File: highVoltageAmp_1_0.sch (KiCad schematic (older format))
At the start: 18 parts, among them U2 OPA211, U3 OPA211

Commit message: Final production board v1.0
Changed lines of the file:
@@
 EESchema Schematic File Version 2
+LIBS:MicroFLiC_DAC_1_0-rescue
 LIBS:power
 LIBS:device
@@
 $EndComp
 Wire Wire Line
-	2800 4000 3050 4000
-Wire Wire Line
-	2800 2800 2800 4150
-Wire Wire Line
-	2800 2800 2900 2800
+	2800 4000 3150 4000
+Wire Wire Line
+	2800 2800 2800 4250
+Wire Wire Line
+	2800 2800 3100 2800
 Connection ~ 2800 4000
 Wire Wire Line
-	3900 2700 4700 2700
-Wire Wire Line
-	4200 2700 4200 4000
-Wire Wire Line
-	4200 4000 3550 4000
-Wire Wire Line
-	2800 4650 2800 4750
+	3700 2700 4700 2700
+Wire Wire Line
+	4200 4000 4200 2700
+Wire Wire Line
+	3450 4000 4200 4000
+Wire Wire Line
+	2800 4550 2800 4750
 $Comp
 L GNDA #PWR031
@@
 U 1 1 55733A0C
 P 3300 4300
+AR Path="/55733A0C" Ref="C14"  Part="1"
+AR Path="/5573337B/55733A0C" Ref="C14"  Part="1"
 F 0 "C14" H 3350 4400 50  0000 L CNN
 F 1 "(10p)" H 3350 4200 50  0000 L CNN
@@
 $EndComp
 Wire Wire Line
-	3500 4300 3650 4300
+	3450 4300 3650 4300
 Wire Wire Line
 	3650 4300 3650 4000
 Connection ~ 3650 4000
 Wire Wire Line
-	3100 4300 2950 4300
+	3150 4300 2950 4300
 Wire Wire Line
 	2950 4300 2950 4000
@@
 U 1 1 55733A19
 P 3650 2200
+AR Path="/55733A19" Ref="C16"  Part="1"
+AR Path="/5573337B/55733A19" Ref="C16"  Part="1"
 F 0 "C16" H 3700 2300 50  0000 L CNN
 F 1 "470p" H 3700 2100 50  0000 L CNN
@@
 U 1 1 55742E4B
 P 3650 1900
+AR Path="/55742E4B" Ref="C15"  Part="1"
+AR Path="/5573337B/55742E4B" Ref="C15"  Part="1"
 F 0 "C15" H 3700 2000 50  0000 L CNN
 F 1 "100n" H 3700 1800 50  0000 L CNN
@@
 $EndComp
 Wire Wire Line
-	3300 1900 3300 2300
+	3300 1900 3300 2400
 $Comp
 L VDD #PWR032
@@
 $EndComp
 Wire Wire Line
-	3450 2200 3400 2200
-Wire Wire Line
-	3400 2200 3300 2300
-Wire Wire Line
-	3450 1900 3350 1900
+	3500 2200 3400 2200
+Wire Wire Line
+	3400 2200 3300 2400
+Wire Wire Line
+	3500 1900 3350 1900
 Wire Wire Line
 	3350 1900 3350 2150
 Wire Wire Line
-	3350 2150 3300 2300
-Wire Wire Line
-	3400 3200 3300 3100
-Wire Wire Line
-	3400 3200 3500 3200
+	3350 2150 3300 2400
+Wire Wire Line
+	3400 3200 3300 3000
+Wire Wire Line
+	3400 3200 3550 3200
 Wire Wire Line
 	3350 3250 3350 3500
 Wire Wire Line
-	3350 3500 3500 3500
-Wire Wire Line
-	3300 3100 3350 3250
-Wire Wire Line
-	3300 3100 3300 3500
+	3350 3500 3550 3500
+Wire Wire Line
+	3300 3000 3350 3250
+Wire Wire Line
+	3300 3000 3300 3500
 $Comp
 L C C17
 U 1 1 55742E4C
 P 3700 3200
+AR Path="/55742E4C" Ref="C17"  Part="1"
+AR Path="/5573337B/55742E4C" Ref="C17"  Part="1"
 F 0 "C17" H 3750 3300 50  0000 L CNN
 F 1 "470p" H 3750 3100 50  0000 L CNN
@@
 U 1 1 55733A4F
 P 3700 3500
+AR Path="/55733A4F" Ref="C18"  Part="1"
+AR Path="/5573337B/55733A4F" Ref="C18"  Part="1"
 F 0 "C18" H 3750 3600 50  0000 L CNN
 F 1 "100n" H 3750 3400 50  0000 L CNN
@@
 $EndComp
 Wire Wire Line
-	3900 3200 4000 3200
+	3850 3200 4000 3200
 Wire Wire Line
 	4000 3200 4000 3600
 Wire Wire Line
-	3900 3500 4000 3500
+	3850 3500 4000 3500
 Connection ~ 4000 3500
 Wire Wire Line
-	3850 2200 3950 2200
+	3800 2200 3950 2200
 Wire Wire Line
 	3950 1900 3950 2300
 Wire Wire Line
-	3850 1900 3950 1900
+	3800 1900 3950 1900
 Connection ~ 3950 2200
 $Comp
@@
 U 1 1 55733A6C
 P 2900 2200
+AR Path="/55733A6C" Ref="C13"  Part="1"
+AR Path="/5573337B/55733A6C" Ref="C13"  Part="1"
 F 0 "C13" H 2950 2300 50  0000 L CNN
 F 1 "10n" H 2950 2100 50  0000 L CNN
@@
 $EndComp
 Wire Wire Line
-	3100 2200 3200 2200
-Wire Wire Line
-	3200 2200 3300 2300
-Wire Wire Line
-	2700 2200 2600 2200
+	3050 2200 3200 2200
+Wire Wire Line
+	3200 2200 3300 2400
+Wire Wire Line
+	2750 2200 2600 2200
 Wire Wire Line
 	2600 2200 2600 3200
@@
 	2600 3200 3200 3200
 Wire Wire Line
-	3200 3200 3300 3100
+	3200 3200 3300 3000
 $Comp
 L R R9
@@
 $EndComp
 Wire Wire Line
-	6900 4000 7150 4000
-Wire Wire Line
-	6900 2800 6900 4150
-Wire Wire Line
-	6900 2800 7000 2800
+	6900 4000 7250 4000
+Wire Wire Line
+	6900 2800 6900 4250
+Wire Wire Line
+	6900 2800 7200 2800
 Connection ~ 6900 4000
 Wire Wire Line
-	8000 2700 8800 2700
-Wire Wire Line
-	8300 2700 8300 4000
-Wire Wire Line
-	8300 4000 7650 4000
-Wire Wire Line
-	6900 4650 6900 4750
+	7800 2700 8800 2700
+Wire Wire Line
+	8300 4000 8300 2700
+Wire Wire Line
+	7550 4000 8300 4000
+Wire Wire Line
+	6900 4550 6900 4750
 $Comp
 L GNDA #PWR036
@@
 U 1 1 55734252
 P 7400 4300
+AR Path="/55734252" Ref="C20"  Part="1"
+AR Path="/5573337B/55734252" Ref="C20"  Part="1"
 F 0 "C20" H 7450 4400 50  0000 L CNN
 F 1 "(10p)" H 7450 4200 50  0000 L CNN
@@
 $EndComp
 Wire Wire Line
-	7600 4300 7750 4300
+	7550 4300 7750 4300
 Wire Wire Line
 	7750 4300 7750 4000
 Connection ~ 7750 4000
 Wire Wire Line
-	7200 4300 7050 4300
+	7250 4300 7050 4300
 Wire Wire Line
 	7050 4300 7050 4000
@@
 U 1 1 5573425E
 P 7750 2200
+AR Path="/5573425E" Ref="C22"  Part="1"
+AR Path="/5573337B/5573425E" Ref="C22"  Part="1"
 F 0 "C22" H 7800 2300 50  0000 L CNN
 F 1 "470p" H 7800 2100 50  0000 L CNN
@@
 U 1 1 55734264
 P 7750 1900
+AR Path="/55734264" Ref="C21"  Part="1"
+AR Path="/5573337B/55734264" Ref="C21"  Part="1"
 F 0 "C21" H 7800 2000 50  0000 L CNN
 F 1 "100n" H 7800 1800 50  0000 L CNN
@@
 $EndComp
 Wire Wire Line
-	7400 1900 7400 2300
+	7400 1900 7400 2400
 $Comp
 L VDD #PWR037
@@
 $EndComp
 Wire Wire Line
-	7550 2200 7500 2200
-Wire Wire Line
-	7500 2200 7400 2300
-Wire Wire Line
-	7550 1900 7450 1900
+	7600 2200 7500 2200
+Wire Wire Line
+	7500 2200 7400 2400
+Wire Wire Line
+	7600 1900 7450 1900
 Wire Wire Line
 	7450 1900 7450 2150
 Wire Wire Line
-	7450 2150 7400 2300
-Wire Wire Line
-	7500 3200 7400 3100
-Wire Wire Line
-	7500 3200 7600 3200
+	7450 2150 7400 2400
+Wire Wire Line
+	7500 3200 7400 3000
+Wire Wire Line
+	7500 3200 7650 3200
 Wire Wire Line
 	7450 3250 7450 3500
 Wire Wire Line
-	7450 3500 7600 3500
-Wire Wire Line
-	7400 3100 7450 3250
-Wire Wire Line
-	7400 3100 7400 3500
+	7450 3500 7650 3500
+Wire Wire Line
+	7400 3000 7450 3250
+Wire Wire Line
+	7400 3000 7400 3500
 $Comp
 L C C23
 U 1 1 5573428A
 P 7800 3200
+AR Path="/5573428A" Ref="C23"  Part="1"
+AR Path="/5573337B/5573428A" Ref="C23"  Part="1"
 F 0 "C23" H 7850 3300 50  0000 L CNN
 F 1 "470p" H 7850 3100 50  0000 L CNN
@@
 U 1 1 55734290
 P 7800 3500
+AR Path="/55734290" Ref="C24"  Part="1"
+AR Path="/5573337B/55734290" Ref="C24"  Part="1"
 F 0 "C24" H 7850 3600 50  0000 L CNN
 F 1 "100n" H 7850 3400 50  0000 L CNN
@@
 $EndComp
 Wire Wire Line
-	8000 3200 8100 3200
+	7950 3200 8100 3200
 Wire Wire Line
 	8100 3200 8100 3600
 Wire Wire Line
-	8000 3500 8100 3500
+	7950 3500 8100 3500
 Connection ~ 8100 3500
 Wire Wire Line
-	7950 2200 8050 2200
+	7900 2200 8050 2200
 Wire Wire Line
 	8050 1900 8050 2300
 Wire Wire Line
-	7950 1900 8050 1900
+	7900 1900 8050 1900
 Connection ~ 8050 2200
 $Comp
@@
 U 1 1 557342AC
 P 7000 2200
+AR Path="/557342AC" Ref="C19"  Part="1"
+AR Path="/5573337B/557342AC" Ref="C19"  Part="1"
 F 0 "C19" H 7050 2300 50  0000 L CNN
 F 1 "10n" H 7050 2100 50  0000 L CNN
@@
 $EndComp
 Wire Wire Line
-	7200 2200 7300 2200
-Wire Wire Line
-	7300 2200 7400 2300
-Wire Wire Line
-	6800 2200 6700 2200
+	7150 2200 7300 2200
+Wire Wire Line
+	7300 2200 7400 2400
+Wire Wire Line
+	6850 2200 6700 2200
 Wire Wire Line
 	6700 2200 6700 3200
@@
 	6700 3200 7300 3200
 Wire Wire Line
-	7300 3200 7400 3100
-Wire Wire Line
-	2900 2600 2000 2600
-Wire Wire Line
-	7000 2600 6100 2600
+	7300 3200 7400 3000
+Wire Wire Line
+	3100 2600 2000 2600
+Wire Wire Line
+	7200 2600 6100 2600
 Text HLabel 2000 2600 0    60   Input ~ 0
 VOUT-0

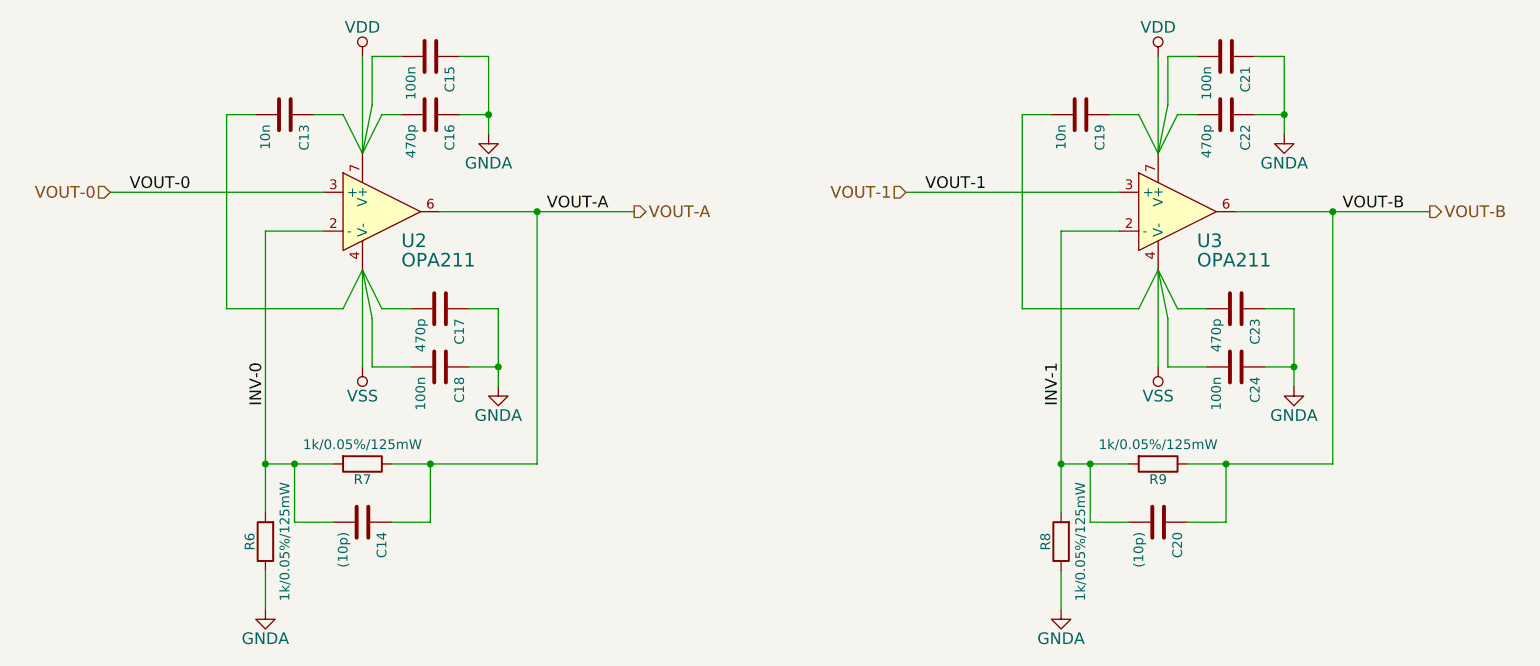
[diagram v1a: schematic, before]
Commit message: Updated part names
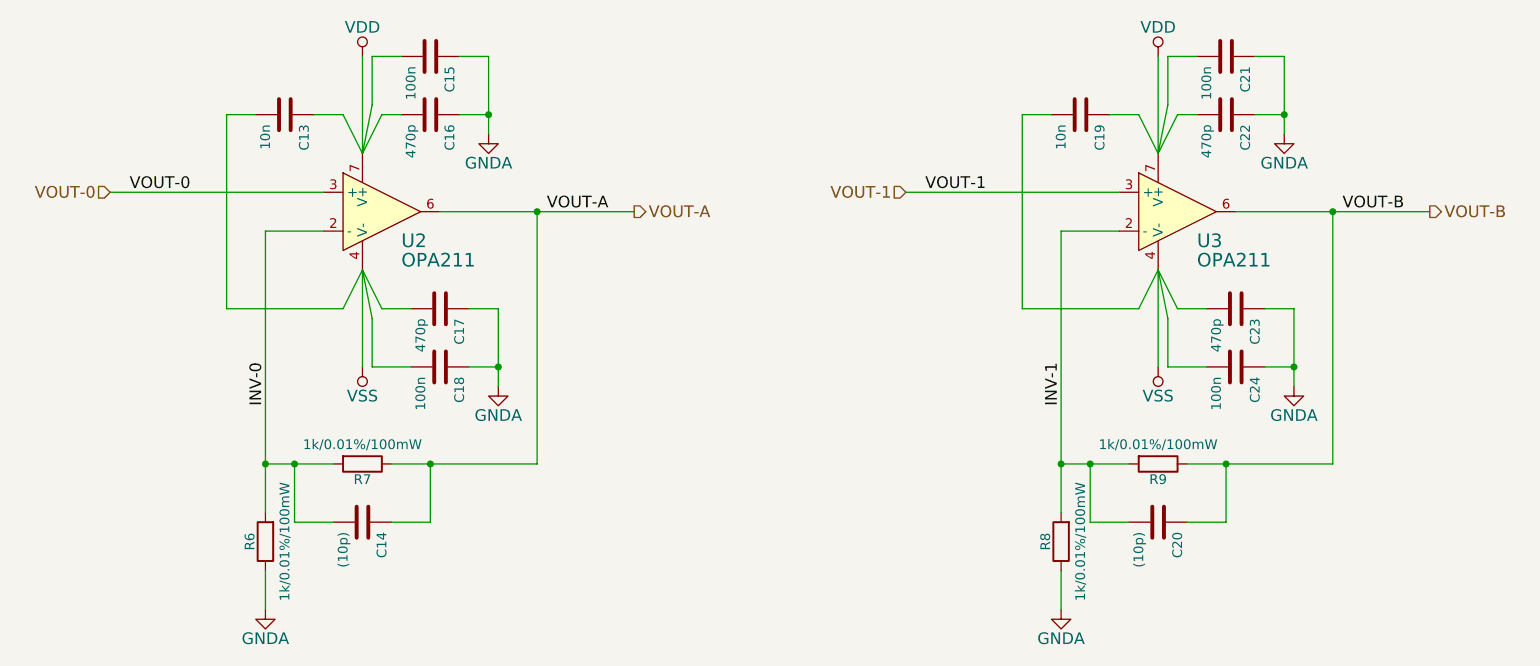
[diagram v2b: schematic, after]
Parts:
- R6, R7, R8, R9: value 1k/0.05%/125mW -> 1k/0.01%/100mW; Manufacturer Panasonic -> Multicomp; Order Code 1688491 -> 2112790; Part Number ERA6ARW102P -> MCTF0805TTX1001
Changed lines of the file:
@@
 P 3300 4000
 F 0 "R7" V 3380 4000 50  0000 C CNN
-F 1 "1k/0.05%/125mW" V 3200 4000 50  0000 C CNN
+F 1 "1k/0.01%/100mW" V 3200 4000 50  0000 C CNN
 F 2 "Resistors_SMD:R_0805" V 3230 4000 30  0001 C CNN
 F 3 "" H 3300 4000 30  0000 C CNN
-F 4 "ERA6ARW102P" V 3300 4000 60  0001 C CNN "Part Number"
-F 5 "Panasonic" V 3300 4000 60  0001 C CNN "Manufacturer"
-F 6 "1688491" V 3300 4000 60  0001 C CNN "Order Code"
+F 4 "MCTF0805TTX1001" V 3300 4000 60  0001 C CNN "Part Number"
+F 5 "Multicomp" V 3300 4000 60  0001 C CNN "Manufacturer"
+F 6 "2112790" V 3300 4000 60  0001 C CNN "Order Code"
 	1    3300 4000
 	0    1    1    0
@@
 P 2800 4400
 F 0 "R6" V 2880 4400 50  0000 C CNN
-F 1 "1k/0.05%/125mW" V 2700 4400 50  0000 C CNN
+F 1 "1k/0.01%/100mW" V 2700 4400 50  0000 C CNN
 F 2 "Resistors_SMD:R_0805" V 2730 4400 30  0001 C CNN
 F 3 "" H 2800 4400 30  0000 C CNN
-F 4 "ERA6ARW102P" V 2800 4400 60  0001 C CNN "Part Number"
-F 5 "Panasonic" V 2800 4400 60  0001 C CNN "Manufacturer"
-F 6 "1688491" V 2800 4400 60  0001 C CNN "Order Code"
+F 4 "MCTF0805TTX1001" V 2800 4400 60  0001 C CNN "Part Number"
+F 5 "Multicomp" V 2800 4400 60  0001 C CNN "Manufacturer"
+F 6 "2112790" V 2800 4400 60  0001 C CNN "Order Code"
 	1    2800 4400
 	-1   0    0    1
@@
 P 7400 4000
 F 0 "R9" V 7480 4000 50  0000 C CNN
-F 1 "1k/0.05%/125mW" V 7300 4000 50  0000 C CNN
+F 1 "1k/0.01%/100mW" V 7300 4000 50  0000 C CNN
 F 2 "Resistors_SMD:R_0805" V 7330 4000 30  0001 C CNN
 F 3 "" H 7400 4000 30  0000 C CNN
-F 4 "ERA6ARW102P" V 7400 4000 60  0001 C CNN "Part Number"
-F 5 "Panasonic" V 7400 4000 60  0001 C CNN "Manufacturer"
-F 6 "1688491" V 7400 4000 60  0001 C CNN "Order Code"
+F 4 "MCTF0805TTX1001" V 7400 4000 60  0001 C CNN "Part Number"
+F 5 "Multicomp" V 7400 4000 60  0001 C CNN "Manufacturer"
+F 6 "2112790" V 7400 4000 60  0001 C CNN "Order Code"
 	1    7400 4000
 	0    1    1    0
@@
 P 6900 4400
 F 0 "R8" V 6980 4400 50  0000 C CNN
-F 1 "1k/0.05%/125mW" V 6800 4400 50  0000 C CNN
+F 1 "1k/0.01%/100mW" V 6800 4400 50  0000 C CNN
 F 2 "Resistors_SMD:R_0805" V 6830 4400 30  0001 C CNN
 F 3 "" H 6900 4400 30  0000 C CNN
-F 4 "ERA6ARW102P" V 6900 4400 60  0001 C CNN "Part Number"
-F 5 "Panasonic" V 6900 4400 60  0001 C CNN "Manufacturer"
-F 6 "1688491" V 6900 4400 60  0001 C CNN "Order Code"
+F 4 "MCTF0805TTX1001" V 6900 4400 60  0001 C CNN "Part Number"
+F 5 "Multicomp" V 6900 4400 60  0001 C CNN "Manufacturer"
+F 6 "2112790" V 6900 4400 60  0001 C CNN "Order Code"
 	1    6900 4400
 	-1   0    0    1
